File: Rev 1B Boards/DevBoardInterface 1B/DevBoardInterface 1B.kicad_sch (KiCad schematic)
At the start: 6 parts, among them J11 Banana 2P, J12 Banana 2P, J13 Banana 2P, J3 Conn_01x01_Pin, J6 JST4_F, J9 Conn_01x01_Pin

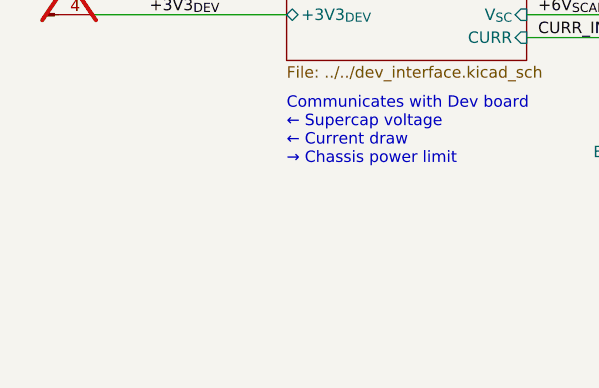
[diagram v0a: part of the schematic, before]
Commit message: Complete dev board interface layout
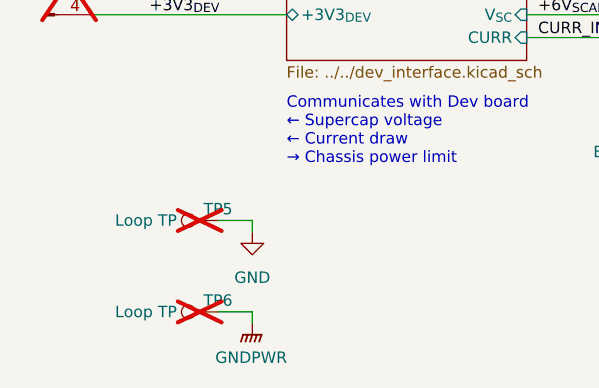
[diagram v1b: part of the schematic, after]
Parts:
- added TP5, TP6: Loop TP, TestPoint:TestPoint_Bridge_Pitch2.0mm_Drill0.7mm, symbol Connector:TestPoint
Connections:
- net GND: now also TP5.1
- net GNDPWR: now also TP6.1

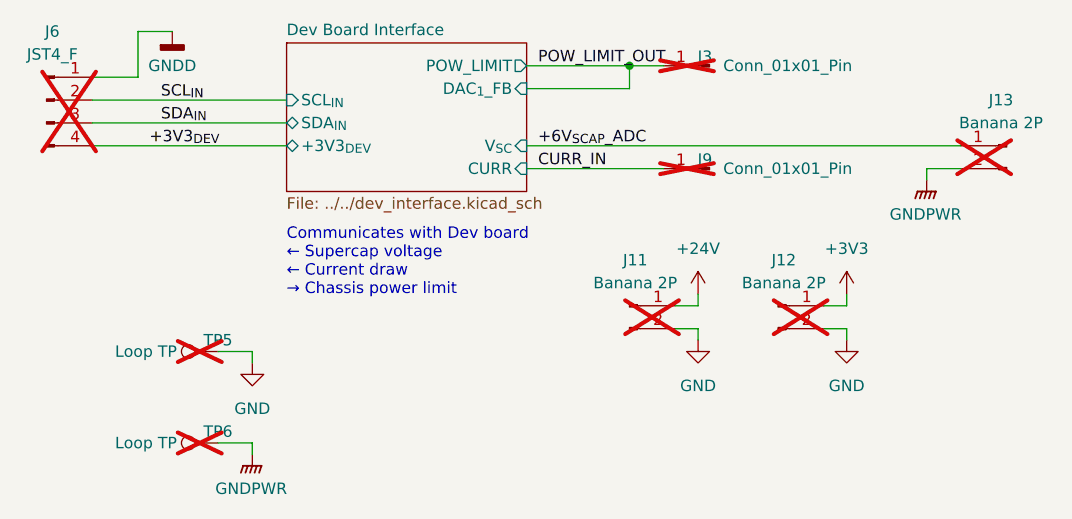
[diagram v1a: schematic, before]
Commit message: Replace most banana jacks with XT connectors
+ update library
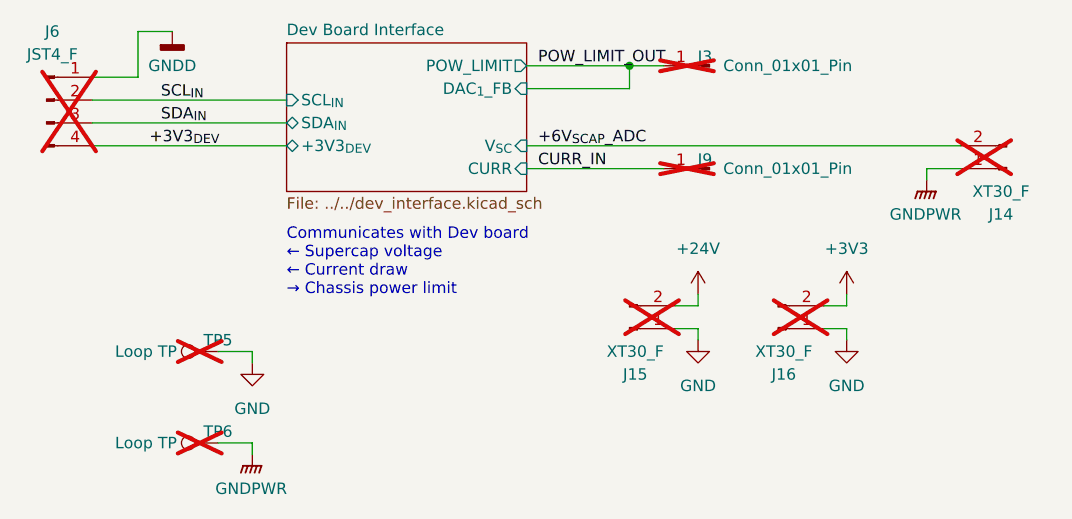
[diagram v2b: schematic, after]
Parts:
- removed J11, J12, J13: Banana 2P, Connector:Banana_Jack_2Pin, symbol Connector:Conn_01x02_Pin
- added J14, J15, J16: XT30_F, Connector_AMASS:AMASS_XT30U-F_1x02_P5.0mm_Vertical, symbol Connector:Conn_01x02_Pin
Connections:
- net +24V: now also J15.2 (Pin_2)
- net +3V3: now also J16.2 (Pin_2)
- net +6V_{SCAP}_ADC: now also J14.2 (Pin_2)
- net GND: now also J15.1 (Pin_1), J16.1 (Pin_1)
- net GNDPWR: now also J14.1 (Pin_1)
